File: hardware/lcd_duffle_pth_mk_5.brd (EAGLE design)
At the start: 80 x 36 mm, 20 parts, among them IC1 ATTINY84, IC2 WS2811

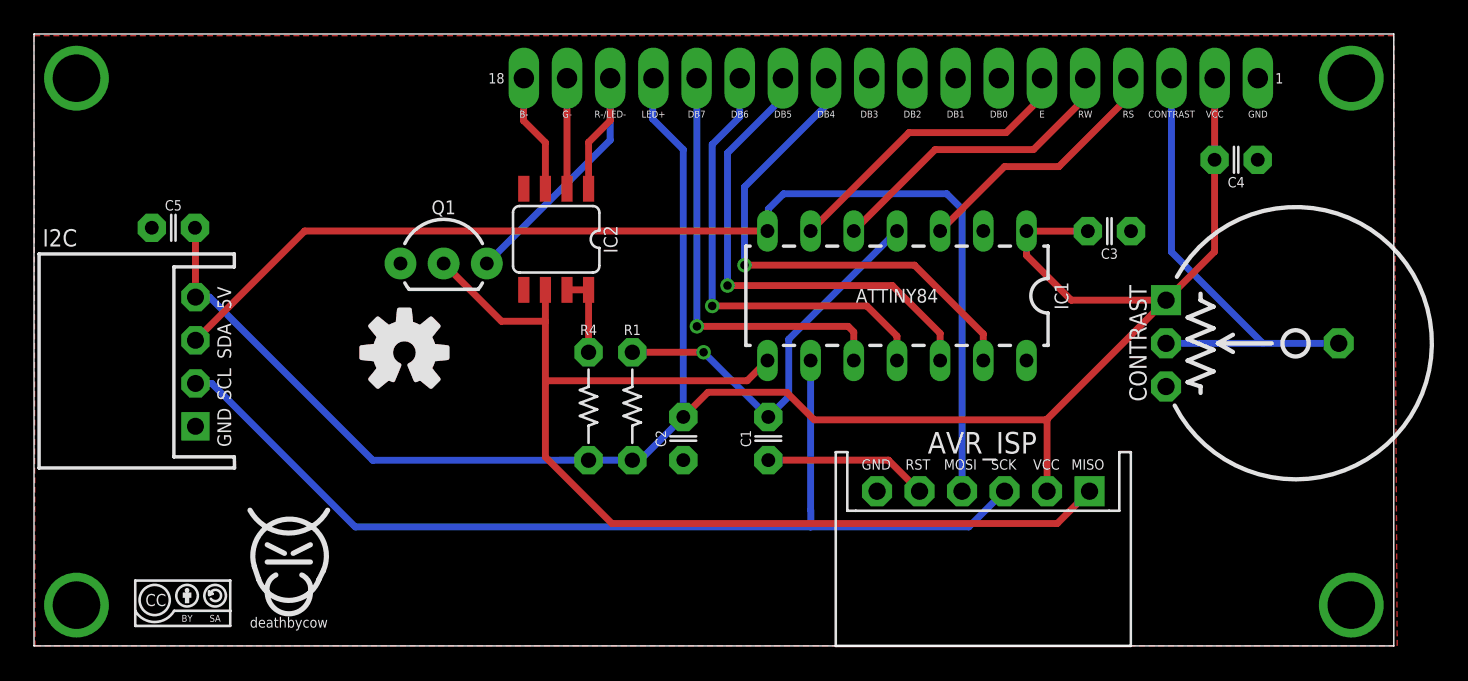
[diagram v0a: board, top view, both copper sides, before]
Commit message: revised board to add i2c pullups, relayout to reduce vias since most were due to poor planning, and remove cap from external reset line as it shouldn't be needed according to atmel's docs
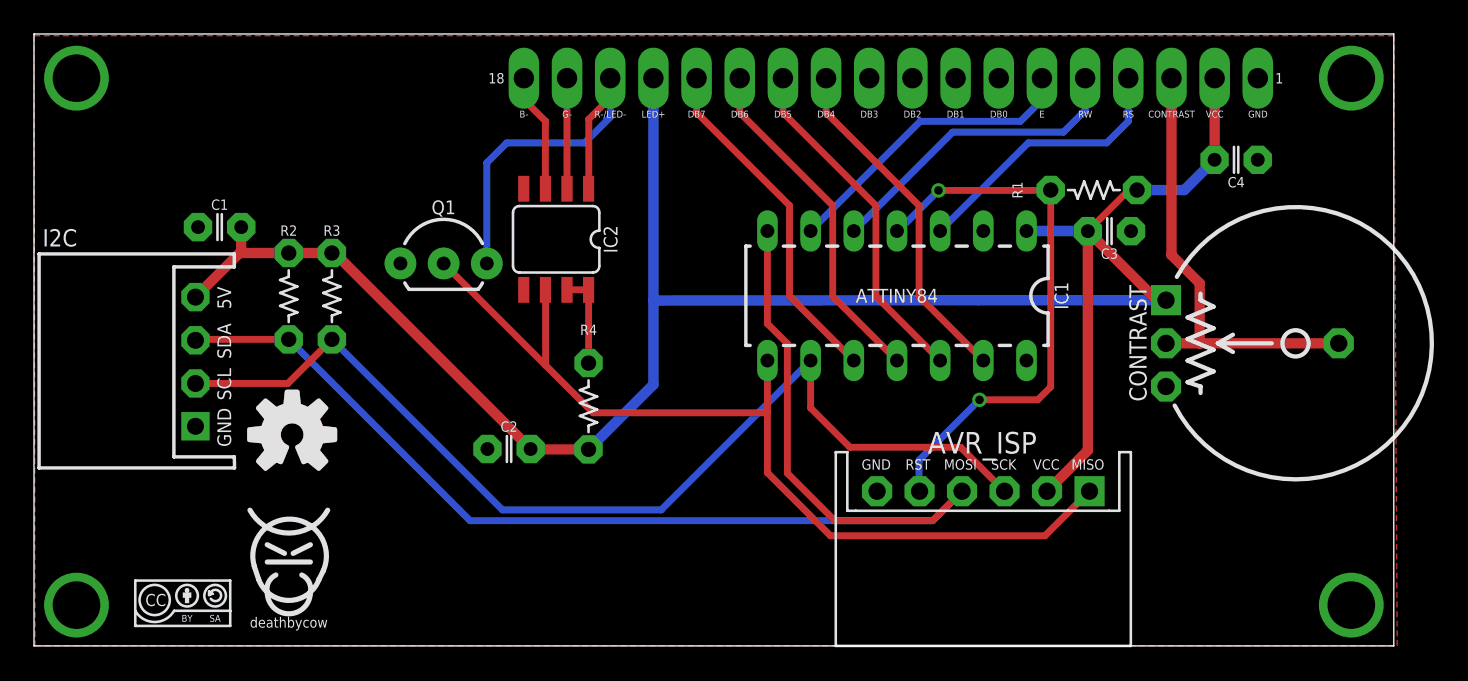
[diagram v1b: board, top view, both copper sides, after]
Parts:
- removed C5: 0.1uF, A_butts:C025-024X044
- added R2, R3: 4.7k, A_butts:RESISTOR-AXIAL-PTH-5.08MM
- I2C: value I2C -> M04JST_XH_RA
- Q1: value (none) -> 1N3904
- moved C1 34.6 mm to (10.9, 24.6), turned to 0 degrees
- moved R1 30.0 mm to (62.4, 26.8), turned to 0 degrees
- moved C2 10.3 mm to (27.9, 11.6), turned to 0 degrees
- moved U$5 8.18 mm to (15.2, 12.4)
- moved U$7 8.18 mm to (15.2, 12.4)
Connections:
- removed net RST: C1.2, IC1.4, R1.P$1
- net 5V: now also C1.2, R2.P$1, R3.P$1; no longer C5.2
- net EXT_RST: now also IC1.4, R1.P$1; no longer C1.1
- net GND: now also C1.1; no longer C5.1
- net SCL: now also R3.P$2
- net SDA: now also R2.P$2
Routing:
- net RST: track 23.7 -> 0.00 mm, vias 1 -> 0
- net EXT_RST: track 9.66 -> 33.0 mm, vias 0 -> 2
- net SDA: track 66.4 -> 77.1 mm
- net LED_CNTL: track 65.2 -> 55.3 mm
- net DB4: track 30.3 -> 20.4 mm, vias 1 -> 0
- net DB5: track 28.8 -> 20.4 mm, vias 1 -> 0
- net DB6: track 27.1 -> 20.4 mm, vias 1 -> 0
- net DB7: track 25.7 -> 20.4 mm, vias 1 -> 0
- net R: track 20.9 -> 23.6 mm
- net CONTRAST: track 28.0 -> 26.4 mm
- net RS: track 15.5 -> 16.3 mm
- net N$2: track 4.94 -> 5.58 mm
